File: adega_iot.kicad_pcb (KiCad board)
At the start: 2 copper layers, 100 x 100 mm, 42 parts, among them J1 Conn_01x03_Pin, J2 Conn_01x02_Pin, J3 Conn_02x05_Odd_Even, J4 Conn_01x03_Pin, J6 Conn_01x03_Pin, Q1 BC548, Q10 BC548, Q11 BC558, Q2 IRF540N, Q3 IRF540N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

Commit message: Preliminary placement
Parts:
- added F1: Fuse, adega_iot:Metaltex_fuse_holder, F.Cu at (36.3, 96.5)
- added J5: Screw_Terminal_01x02, adega_iot:HANDSON_KF301-2P, F.Cu at (5.08, 96.5)
- added J7: Screw_Terminal_01x02, adega_iot:HANDSON_KF301-2P, F.Cu at (45.7, 96.5)
- added J8: Conn_01x02_Pin, Connector_PinHeader_2.54mm:PinHeader_1x02_P2.54mm_Vertical, F.Cu at (88.9, 86.4)
- added J9: Conn_01x02_Pin, Connector_PinHeader_2.54mm:PinHeader_1x02_P2.54mm_Vertical, F.Cu at (71.1, 86.4)
- added SW1: SW_Push, Button_Switch_THT:SW_PUSH_6mm_H7.3mm, F.Cu at (10.2, 19.4)
- added SW2: SW_Push, Button_Switch_THT:SW_PUSH_6mm_H7.3mm, F.Cu at (10.2, 9.87)
- Q1, Q10, Q11, Q4, Q5, Q6, Q7, Q8, Q9: footprint Package_TO_SOT_THT:TO-92_Inline -> Package_TO_SOT_THT:TO-92_Inline_Wide
- moved U2 81.4 mm to (40.6, 7.62), turned to 0 degrees
- moved U3 71.2 mm to (3.81, 86.4), turned to 90 degrees
- moved J4 66.6 mm to (33.0, 63.5), turned to 180 degrees
- moved R6 65.7 mm to (96.5, 17.8), turned to 90 degrees
- moved J3 59.7 mm to (30.5, 38.1), turned to 180 degrees
- moved R5 58.6 mm to (88.9, 16.5), turned to 90 degrees
- moved R8 57.6 mm to (35.6, 78.7), turned to 90 degrees
- moved C3 54.7 mm to (5.08, 38.1)
- moved C5 51.9 mm to (94.0, 35.6), turned to -90 degrees
- moved R4 50.8 mm to (81.3, 16.5), turned to 90 degrees
- moved C2 50.6 mm to (33.0, 7.62), turned to -90 degrees
- moved R2 49.9 mm to (16.5, 7.33)
- moved R12 49.2 mm to (91.4, 58.4), turned to -90 degrees
- moved R1 42.4 mm to (15.2, 14.9)
- moved Q1 41.4 mm to (38.1, 78.7)
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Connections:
- C4 pad 1: +3V3 -> +5V

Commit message: partial routing
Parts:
- removed C5: 100n, Capacitor_THT:C_Disc_D7.5mm_W4.4mm_P5.00mm
- added H1: MountingHole, MountingHole:MountingHole_2mm, F.Cu at (96.0, 10.8)
- added H10: MountingHole, MountingHole:MountingHole_2mm, F.Cu at (96.0, 53.8)
- added H11: MountingHole, MountingHole:MountingHole_2mm, F.Cu at (96.0, 35.8)
- added H12: MountingHole, MountingHole:MountingHole_2mm, F.Cu at (96.0, 59.8)
- added H13: MountingHole, MountingHole:MountingHole_3.2mm_M3, F.Cu at (14.5, 5.00)
- added H14: MountingHole, MountingHole:MountingHole_3.2mm_M3, F.Cu at (85.5, 5.00)
- added H15: MountingHole, MountingHole:MountingHole_3.2mm_M3, F.Cu at (85.5, 95.0)
- added H16: MountingHole, MountingHole:MountingHole_3.2mm_M3, F.Cu at (143.3, 92.9)
- added H2: MountingHole, MountingHole:MountingHole_2mm, F.Cu at (96.0, 24.8)
- added H3: MountingHole, MountingHole:MountingHole_2mm, F.Cu at (96.0, 4.82)
- added H4: MountingHole, MountingHole:MountingHole_2mm, F.Cu at (96.0, 18.8)
- added H5: MountingHole, MountingHole:MountingHole_2mm, F.Cu at (29.5, 94.8)
- added H6: MountingHole, MountingHole:MountingHole_2mm, F.Cu at (55.5, 94.8)
- added H7: MountingHole, MountingHole:MountingHole_2mm, F.Cu at (61.5, 94.8)
- added H8: MountingHole, MountingHole:MountingHole_2mm, F.Cu at (35.5, 94.8)
- added H9: MountingHole, MountingHole:MountingHole_2mm, F.Cu at (96.0, 41.8)
- added J10: Conn_01x02_Pin, Connector_PinHeader_2.54mm:PinHeader_1x02_P2.54mm_Vertical, F.Cu at (63.9, 37.9)
- moved R6 75.6 mm to (20.9, 18.7)
- moved R5 73.0 mm to (15.9, 18.7)
- moved D2 72.6 mm to (8.66, 3.52)
- moved R4 72.4 mm to (8.92, 17.7)
- moved D4 71.9 mm to (24.7, 3.55)
- moved D1 70.7 mm to (3.00, 3.52)
- moved R3 69.6 mm to (4.06, 17.7)
- moved D3 68.6 mm to (20.3, 3.55)
- moved Q9 56.3 mm to (75.9, 26.3), turned to -90 degrees
- moved J8 47.6 mm to (90.0, 38.8), turned to 180 degrees
- moved R12 43.4 mm to (64.9, 24.1)
- moved Q8 40.7 mm to (70.3, 35.0), turned to 90 degrees
- moved Q6 40.6 mm to (75.9, 39.0), turned to 90 degrees
- moved R10 37.1 mm to (76.7, 41.9), turned to 180 degrees
- moved J2 36.0 mm to (90.0, 7.82)
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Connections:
- J4 pad 2: /GPIO_34 -> /GPIO_16
- U2 pad 10: unconnected-(U2-DAC_2/ADC2_CH9/GPIO26-Pad10) -> /SW1
- U2 pad 24: /LED3 -> /FAN1
- U2 pad 25: unconnected-(U2-GPIO0/BOOT/ADC2_CH1-Pad25) -> /BOOT
- U2 pad 27: unconnected-(U2-GPIO16-Pad27) -> /GPIO_16
- U2 pad 29: /DS18B20 -> /FAN2
- U2 pad 30: /FAN1 -> unconnected-(U2-GPIO18-Pad30)
- U2 pad 31: /LED0 -> /DS18B20
- U2 pad 33: /LED1 -> unconnected-(U2-GPIO21-Pad33)
- U2 pad 36: /LED2 -> unconnected-(U2-GPIO22-Pad36)
- U2 pad 37: /FAN2 -> unconnected-(U2-GPIO23-Pad37)
- U2 pad 5: /GPIO_34 -> /LED0
- U2 pad 6: unconnected-(U2-VDET_2/GPIO35/ADC1_CH7-Pad6) -> /LED1
- U2 pad 7: /SW1 -> /LED2
- U2 pad 8: /SW2 -> /LED3
- U2 pad 9: unconnected-(U2-DAC_1/ADC2_CH8/GPIO25-Pad9) -> /SW2
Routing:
- net GND: track 0.00 -> 420.5 mm
- net +12V: track 0.00 -> 159.0 mm
- net /MOSFET_GATE: track 0.00 -> 73.6 mm
- net /RST: track 0.00 -> 56.9 mm
- net Net-(J7-Pin_2): track 0.00 -> 56.6 mm
- net /GPIO_16: track 0.00 -> 55.1 mm
- net +5V: track 0.00 -> 41.2 mm
- net /TEMP_PELTIER: track 0.00 -> 40.7 mm
- net /SW2: track 0.00 -> 40.6 mm
- net /SW1: track 0.00 -> 39.7 mm
- net /DS18B20: track 0.00 -> 35.1 mm
- net /LED0: track 0.00 -> 32.1 mm
- net /LED1: track 0.00 -> 26.1 mm
- net Net-(Q10-C): track 0.00 -> 23.9 mm
- net Net-(J2-Pin_2): track 0.00 -> 23.9 mm
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
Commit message: Routing Progress
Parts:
- removed D5: D_Zener, Diode_THT:D_A-405_P7.62mm_Horizontal
- removed J5: Screw_Terminal_01x02, adega_iot:HANDSON_KF301-2P
- added ?: , , F.Cu at (17.8, 37.3)
- J3: value Conn_02x05_Odd_Even -> Screw_Terminal_01x02; footprint Connector_PinHeader_2.54mm:PinHeader_2x05_P2.54mm_Vertical -> adega_iot:HANDSON_KF301-2P
- moved J3 41.5 mm to (32.5, 79.8), turned to 0 degrees
- moved R9 6.81 mm to (49.8, 27.0)
- moved C1 2.71 mm to (30.5, 50.0)
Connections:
- C4 pad 1: +5V -> +3V3
- F1 pad 2: Net-(J5-Pin_1) -> Net-(J3-Pin_2)
- J1 pad 1: +5V -> +3V3
- J2 pad 1: +5V -> +3V3
- J3 pad 1: +3V3 -> GND
- J3 pad 2: /TMS -> Net-(J3-Pin_2)
- U1 pad 4: +5V -> +3V3
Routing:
- net +3V3: track 8.29 -> 104.7 mm
- net /RST: track 56.9 -> 0.00 mm
- net GND: track 420.5 -> 392.5 mm, vias 0 -> 13
- net /TCK: track 18.4 -> 0.00 mm
- net Net-(J5-Pin_1): track 18.1 -> 0.00 mm
- net Net-(J3-Pin_2): track 0.00 -> 18.1 mm
- net /PELTIER_POWER: track 9.99 -> 16.9 mm
- net /MOSFET_GATE: track 73.6 -> 68.1 mm
- net /TEMP_PELTIER: track 40.7 -> 35.3 mm
- net /GPIO_16: track 55.1 -> 51.2 mm
- net Net-(Q4-B): track 18.5 -> 21.4 mm
- net +12V: track 159.0 -> 161.5 mm
- net +5V: track 41.2 -> 40.3 mm
- added copper zone on F.Cu, net +12V
- added copper zone on B.Cu, net GND
- added copper zone on F.Cu, net GND
- added copper zone on B.Cu, net Net-(J3-Pin_2)
- added copper zone on B.Cu, net Net-(J7-Pin_2)

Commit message: routing progress
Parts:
- added ?: , , F.Cu at (94.0, 14.5)
- added ?: , , F.Cu at (53.1, 1.78)
- added ?: , , F.Cu at (1.80, 88.1)
- added ?: , , F.Cu at (78.8, 87.6)
- added ?: , , F.Cu at (42.9, 98.0)
- added ?: , , F.Cu at (47.3, 98.0)
- added ?: , , F.Cu at (37.4, 34.0)
- added ?: , , F.Cu at (61.5, 85.9)
- added ?: , , F.Cu at (51.8, 80.0)
- added ?: , , F.Cu at (5.10, 88.1)
- added ?: , , F.Cu at (75.2, 85.6)
- added ?: , , F.Cu at (66.3, 73.7)
- added ?: , , F.Cu at (85.9, 69.3)
- added ?: , , F.Cu at (89.7, 77.2)
- added ?: , , F.Cu at (29.5, 34.0)
- added ?: , , F.Cu at (45.7, 7.37)
- added ?: , , F.Cu at (55.9, 84.8)
- added ?: , , F.Cu at (53.4, 17.3)
- added ?: , , F.Cu at (86.9, 13.2)
- moved ? 3.31 mm to (19.6, 40.1)
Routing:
- net Net-(J3-Pin_2): track 18.1 -> 0.00 mm
- net GND: vias 13 -> 0
- added copper zone on B.Cu, net +12V

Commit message: routing updates
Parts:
- added Q12: IRF540N, Package_TO_SOT_THT:TO-220-3_Vertical, F.Cu at (85.1, 38.9)
- added Q13: IRF540N, Package_TO_SOT_THT:TO-220-3_Vertical, F.Cu at (85.1, 56.9)
- moved ? 3.05 mm to (52.9, 84.8)
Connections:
- J8 pad 1: Net-(J8-Pin_1) -> +12V
- J8 pad 2: GND -> Net-(J8-Pin_2)
- J9 pad 1: Net-(J9-Pin_1) -> +12V
- J9 pad 2: GND -> Net-(J9-Pin_2)
- Q11 pad 3: Net-(J9-Pin_1) -> Net-(Q11-E)
- Q6 pad 3: Net-(J8-Pin_1) -> Net-(Q12-G)
- Q7 pad 3: Net-(J9-Pin_1) -> Net-(Q11-E)
- Q9 pad 3: Net-(J8-Pin_1) -> Net-(Q12-G)
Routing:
- net GND: track 392.5 -> 360.9 mm
- net +12V: track 161.5 -> 191.4 mm
- net Net-(J9-Pin_1): track 18.8 -> 0.00 mm
- net Net-(J8-Pin_1): track 18.6 -> 0.00 mm
- net Net-(Q12-G): track 0.00 -> 15.2 mm
- net Net-(Q11-E): track 0.00 -> 14.7 mm
- net Net-(J9-Pin_2): track 0.00 -> 4.92 mm
- net Net-(J8-Pin_2): track 0.00 -> 4.91 mm
- net /GPIO_16: track 51.2 -> 49.6 mm

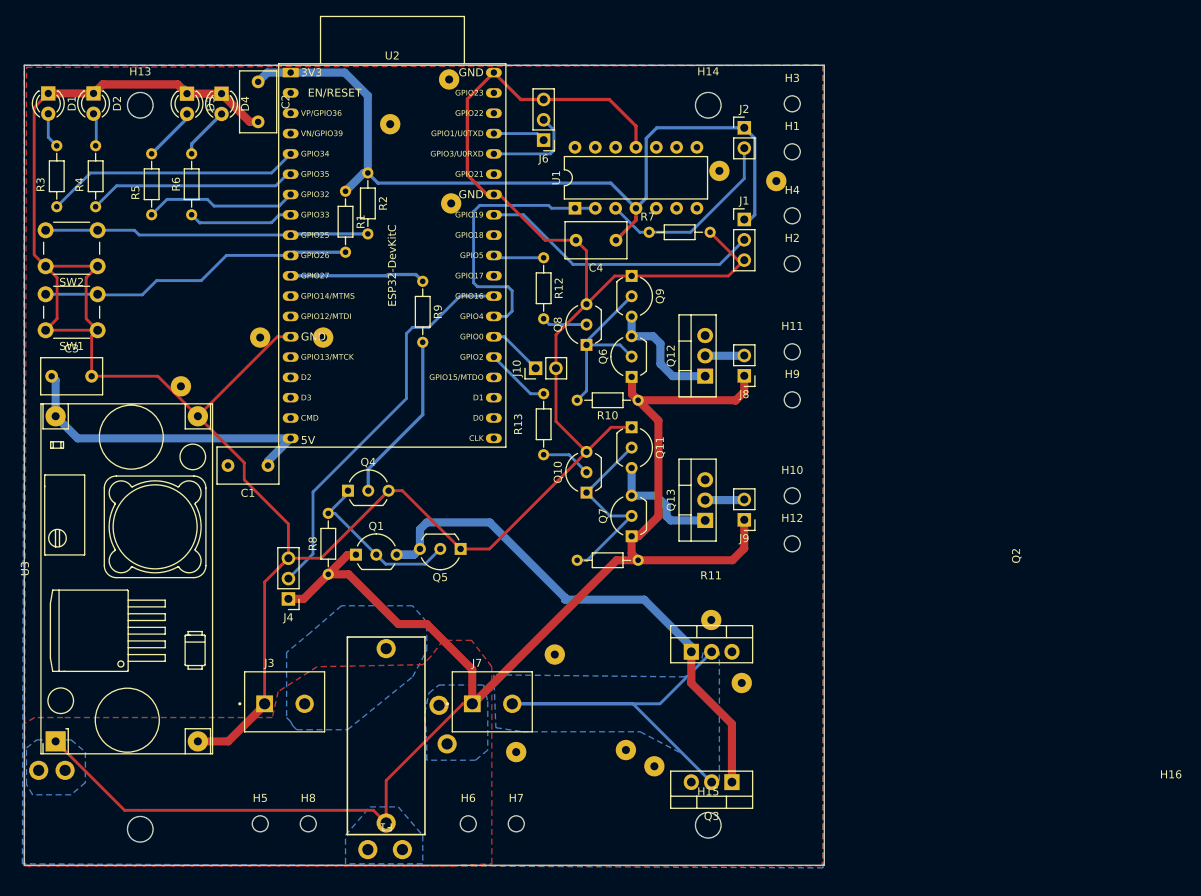
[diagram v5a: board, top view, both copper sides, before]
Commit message: DRC and Teardrops
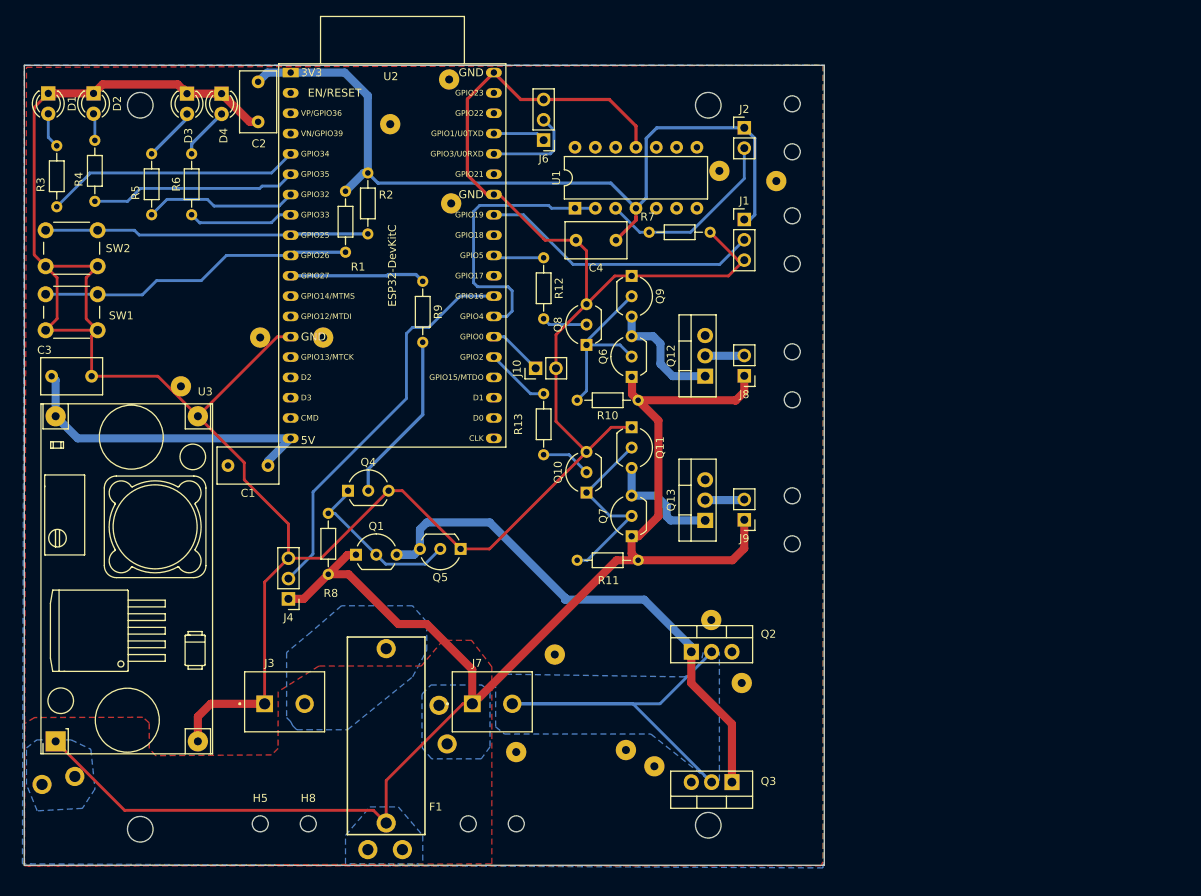
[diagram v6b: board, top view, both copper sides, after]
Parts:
- moved ? 1.81 mm to (2.22, 89.9)
- moved ? 1.44 mm to (6.32, 88.9)
- moved R4 0.68 mm to (8.82, 17.0)
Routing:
- net /MOSFET_GATE: track 68.1 -> 67.4 mm
- net Net-(D2-A): track 4.03 -> 3.39 mm

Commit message: Added a pullup to DS18B20
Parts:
- added ?: , , F.Cu at (71.7, 20.3)
- added R14: 1k, Resistor_THT:R_Axial_DIN0204_L3.6mm_D1.6mm_P7.62mm_Horizontal, F.Cu at (78.0, 23.1)
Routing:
- net +3V3: track 104.7 -> 112.2 mm
- net /DS18B20: track 35.1 -> 40.1 mm

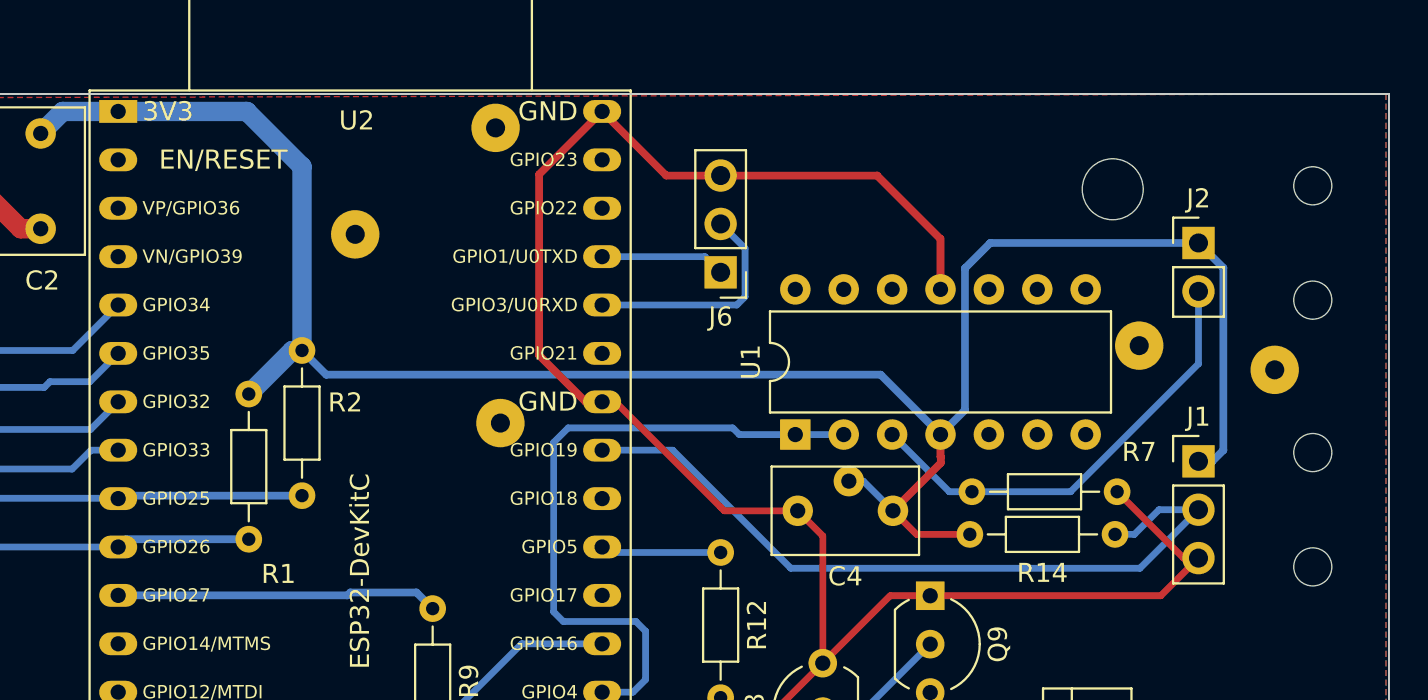
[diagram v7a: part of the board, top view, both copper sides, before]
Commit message: Reset Button and NTC pullup
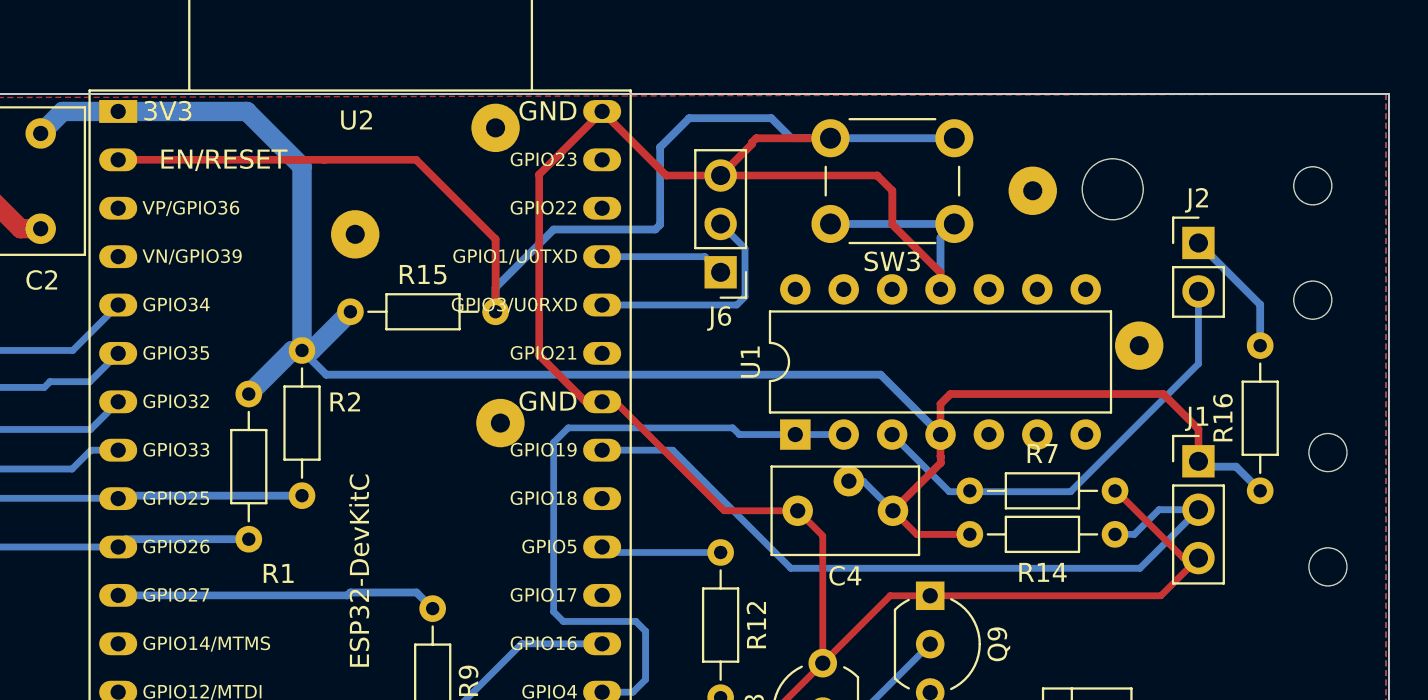
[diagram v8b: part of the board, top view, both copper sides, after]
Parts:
- added R15: 10k, Resistor_THT:R_Axial_DIN0204_L3.6mm_D1.6mm_P7.62mm_Horizontal, F.Cu at (45.5, 11.4)
- added R16: 1k, Resistor_THT:R_Axial_DIN0204_L3.6mm_D1.6mm_P7.62mm_Horizontal, F.Cu at (93.2, 20.8)
- added SW3: SW_Push, Button_Switch_THT:SW_PUSH_6mm_H7.3mm, F.Cu at (77.2, 6.82)
- moved ? 15.8 mm to (81.3, 5.08)
- moved H2 0.80 mm to (96.8, 24.8)
- moved H4 0.80 mm to (96.8, 18.8)
- moved R7 0.12 mm to (78.0, 20.8)
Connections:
- J2 pad 1: +3V3 -> Net-(J2-Pin_1)
- U2 pad 12: /TMS -> unconnected-(U2-MTMS/GPIO14/ADC2_CH6-Pad12)
- U2 pad 13: /TDI -> unconnected-(U2-MTDI/GPIO12/ADC2_CH5-Pad13)
- U2 pad 15: /TCK -> unconnected-(U2-MTCK/GPIO13/ADC2_CH4-Pad15)
- U2 pad 23: /TDO -> unconnected-(U2-MTDO/GPIO15/ADC2_CH3-Pad23)
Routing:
- net /RST: track 0.00 -> 57.2 mm
- net GND: track 360.8 -> 377.7 mm
- net +3V3: track 112.2 -> 102.3 mm
- net Net-(J2-Pin_1): track 0.00 -> 6.73 mm
